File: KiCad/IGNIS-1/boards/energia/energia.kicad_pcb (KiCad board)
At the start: 2 copper layers, 62 x 62 mm, 8 parts, among them J40 Backplane, U3 Boost_5V

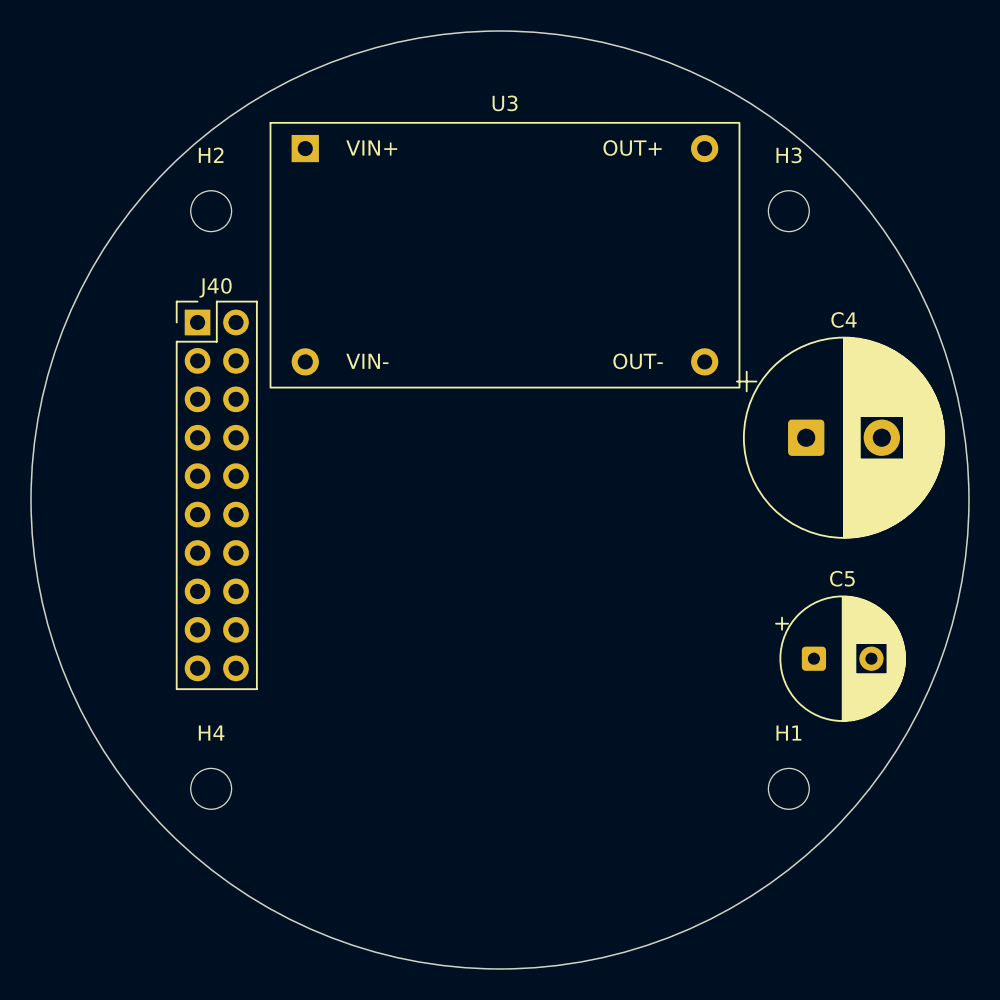
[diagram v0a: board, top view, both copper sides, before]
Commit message: 5 boards separados, falta ajustar dimensiones de BME280 y MQ-135
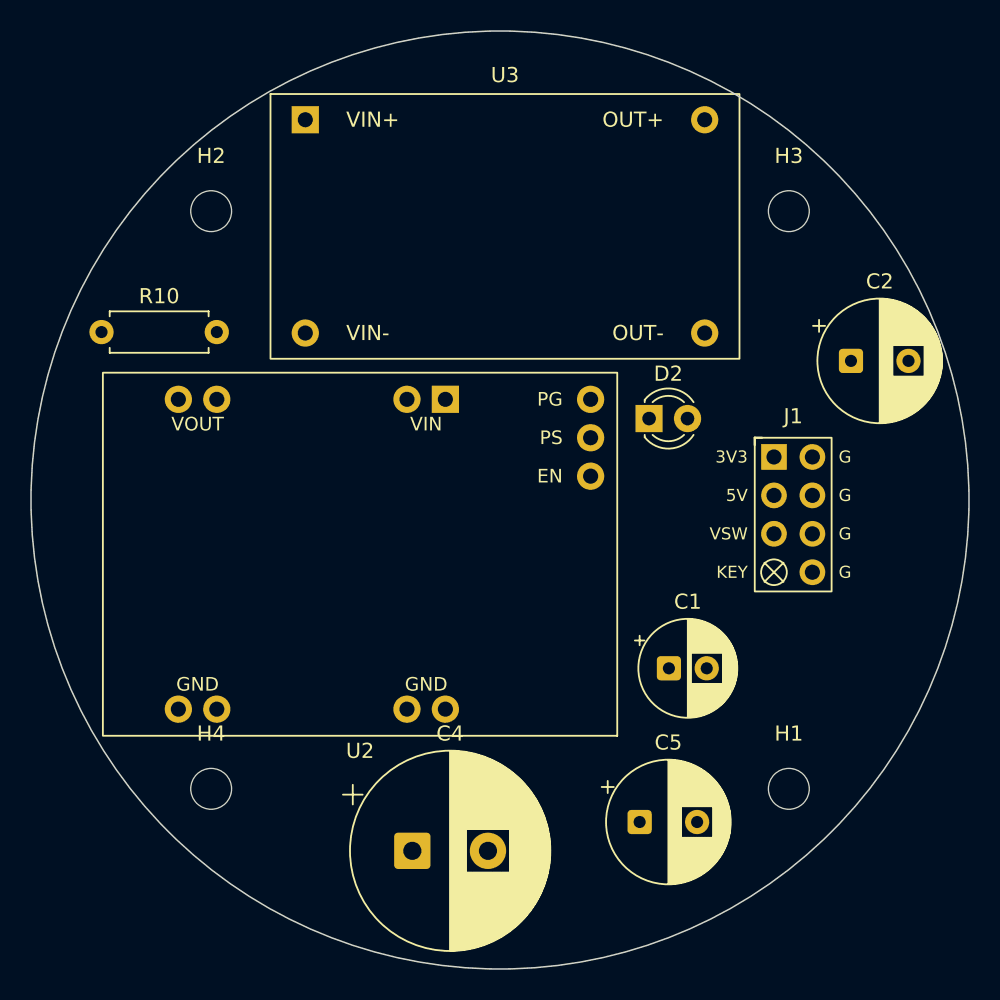
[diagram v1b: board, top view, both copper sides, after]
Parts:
- removed J40: Backplane, Connector_PinHeader_2.54mm:PinHeader_2x10_P2.54mm_Vertical
- added C1: 22uF, Capacitor_THT:CP_Radial_D6.3mm_P2.50mm, F.Cu at (111.2, 111.1)
- added C2: 100uF, Capacitor_THT:CP_Radial_D8.0mm_P3.80mm, F.Cu at (123.2, 90.8)
- added D2: PWR_grn, LED_THT:LED_D3.0mm, F.Cu at (109.9, 94.6)
- added J1: J_PWR_2x4, IGNIS1:J_PWR_2x4_Keyed, F.Cu at (119.4, 101.0)
- added R10: 1k, Resistor_THT:R_Axial_DIN0207_L6.3mm_D2.5mm_P7.62mm_Horizontal, F.Cu at (73.7, 88.9)
- added U2: TPS63020, IGNIS1:TPS63020_module, F.Cu at (90.8, 103.6)
- moved C4 37.7 mm to (94.2, 123.2)
- moved C5 15.8 mm to (109.2, 121.3)
- moved U3 1.90 mm to (100.3, 81.9)

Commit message: Se agregaron tracks. PCB Cerebro libre de errores.
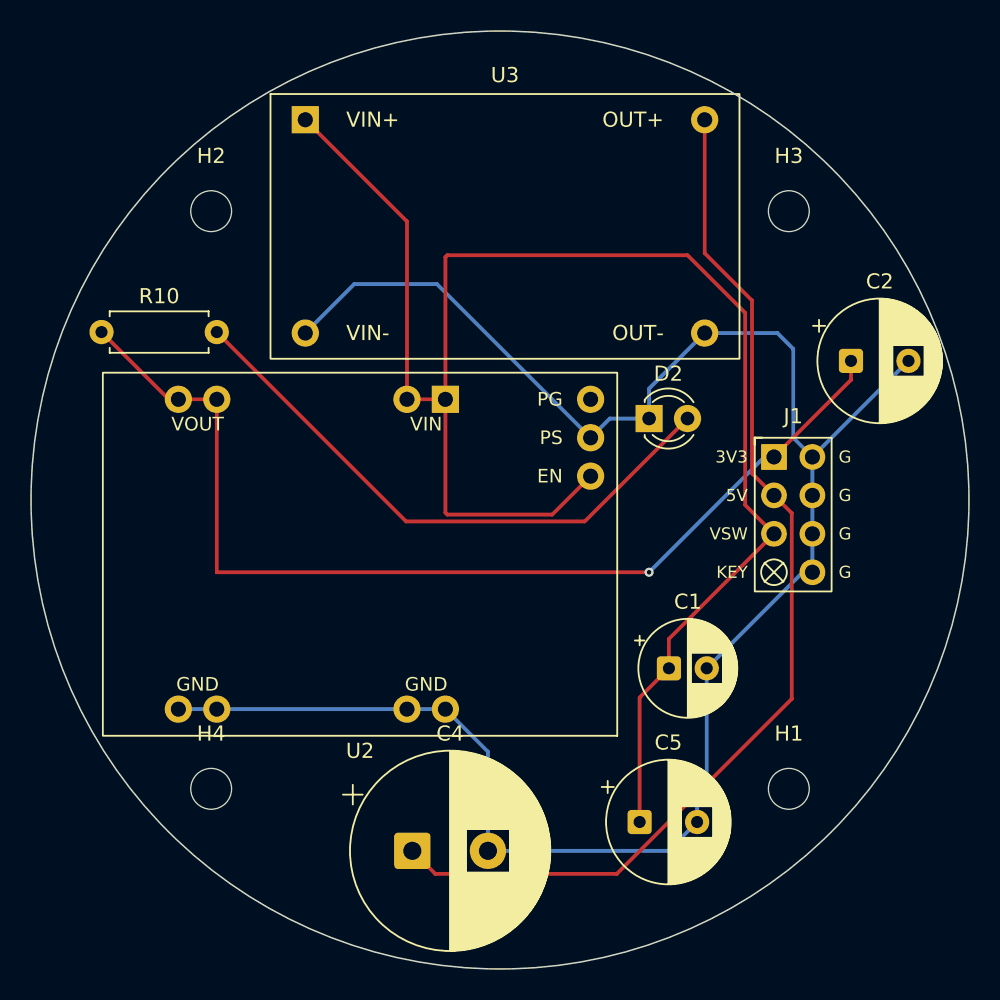
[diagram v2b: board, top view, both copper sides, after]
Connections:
- J1 pad 1: unconnected-(J1-+3V3-Pad1) -> +3V3
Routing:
- net GND: track 0.00 -> 129.4 mm
- net VSW: track 0.00 -> 111.0 mm
- net +5V: track 0.00 -> 71.6 mm
- net +3V3: track 0.00 -> 69.3 mm, vias 0 -> 1
- net Net-(D2-A): track 0.00 -> 39.1 mm

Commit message: Todos los boards pasan el check, tracks completos
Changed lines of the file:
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@@
 		(at 80.908 119.092)
 		(property "Reference" "H4"
-			(at 0 -3.65 0)
+			(at 3.928 -2.252 0)
 			(layer "F.SilkS")
 			(effects
@@
 		(tags "CP Radial series Radial pin pitch 5.00mm diameter 13mm height 20mm Electrolytic Capacitor")
 		(property "Reference" "C4"
-			(at 2.5 -7.75 0)
+			(at 8.411215 -5.715 0)
 			(layer "F.SilkS")
 			(effects
